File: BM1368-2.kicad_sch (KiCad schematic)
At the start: 39 parts, among them U12 BM1368_mode1, U13 BM1368_mode1

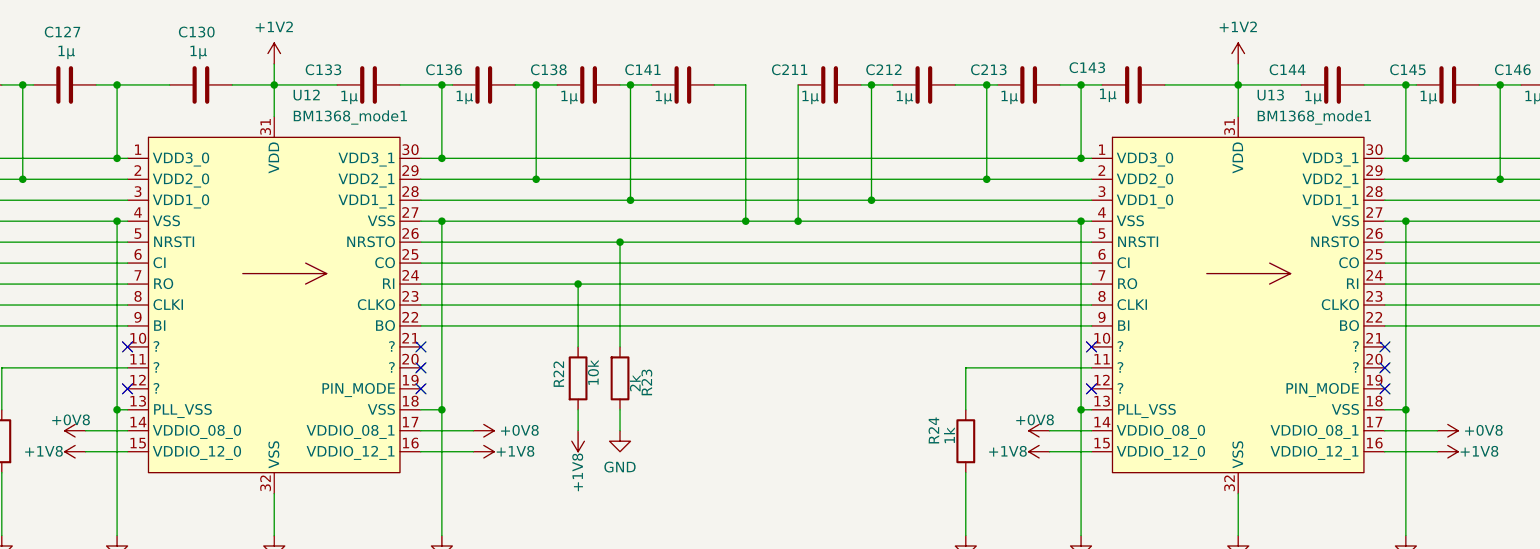
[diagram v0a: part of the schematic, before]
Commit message: Added 4th Phase Buck
Started to add 4th Phase for the Buck, implementing BM1370 footprint etc
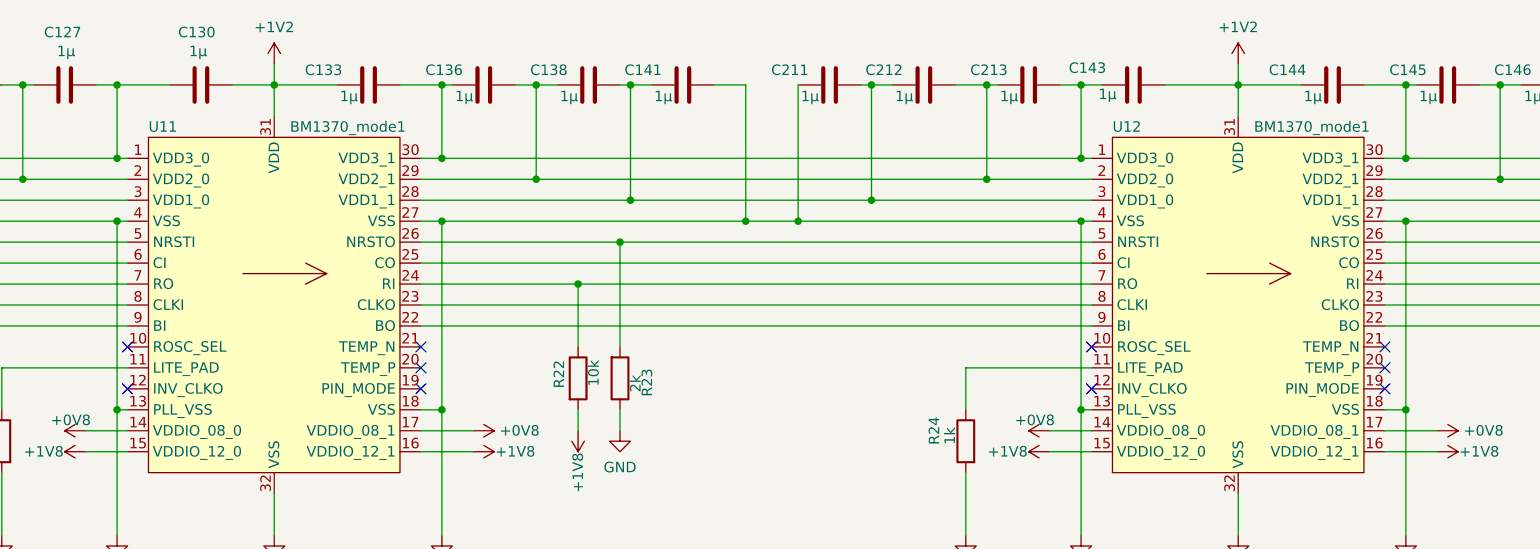
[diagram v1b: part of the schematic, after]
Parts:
- removed U12, U13: BM1368_mode1, myfootprints:bm1368-package-modified, symbol mylib7:BM1368_mode1
- added U11, U12: BM1370_mode1, Nerd8:BM1370, symbol bitaxe:BM1370_mode1
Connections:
- net +0V8: now also U11.14 (VDDIO_08_0), U11.17 (VDDIO_08_1), U12.14 (VDDIO_08_0), U12.17 (VDDIO_08_1)
- net +1V2: now also U11.31 (VDD), U12.31 (VDD)
- net +1V8: now also U11.15 (VDDIO_12_0), U11.16 (VDDIO_12_1), U12.15 (VDDIO_12_0), U12.16 (VDDIO_12_1)
- net BI: now also U11.9 (BI)
- net BO: now also U12.22 (BO)
- net CI: now also U11.6 (CI)
- net CLKI: now also U11.8 (CLKI)
- net CLKO: now also U12.23 (CLKO)
- net CO: now also U12.25 (CO)
- net GND: now also U11.13 (PLL_VSS), U11.18 (VSS), U11.27 (VSS), U11.32 (VSS), U11.4 (VSS), U12.13 (PLL_VSS), U12.18 (VSS), U12.27 (VSS), U12.32 (VSS), U12.4 (VSS)
- net NRSTI: now also U11.5 (NRSTI)
- net NRSTO: now also U12.26 (NRSTO)
- net RI: now also U12.24 (RI)
- net RO: now also U11.7 (RO)
- net U11-VDD1_1: now also U11.3 (VDD1_0)
- net U11-VDD2_1: now also U11.2 (VDD2_0)
- net U11-VDD3_1: now also U11.1 (VDD3_0)
- net U13-VDD1_1: now also U12.28 (VDD1_1)
- net U13-VDD2_1: now also U12.29 (VDD2_1)
- net U13-VDD3_1: now also U12.30 (VDD3_1)
- net at C133.2, C136.1, C143.1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: now also U11.30 (VDD3_1), U12.1 (VDD3_0)
- net at C136.2, C138.1, C212.2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: now also U11.29 (VDD2_1), U12.2 (VDD2_0)
- net at C138.2, C141.1, C211.2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: now also U11.28 (VDD1_1), U12.3 (VDD1_0)
- net at R24.1: now also U12.11 (LITE_PAD)
- net at R23.2: now also U11.26 (NRSTO), U12.5 (NRSTI)
- net at R22.1: now also U11.24 (RI), U12.7 (RO)
- net at R21.1: now also U11.11 (LITE_PAD)
- new net: U11.25 (CO), U12.6 (CI)
- new net: U11.23 (CLKO), U12.8 (CLKI)
- new net: U11.22 (BO), U12.9 (BI)

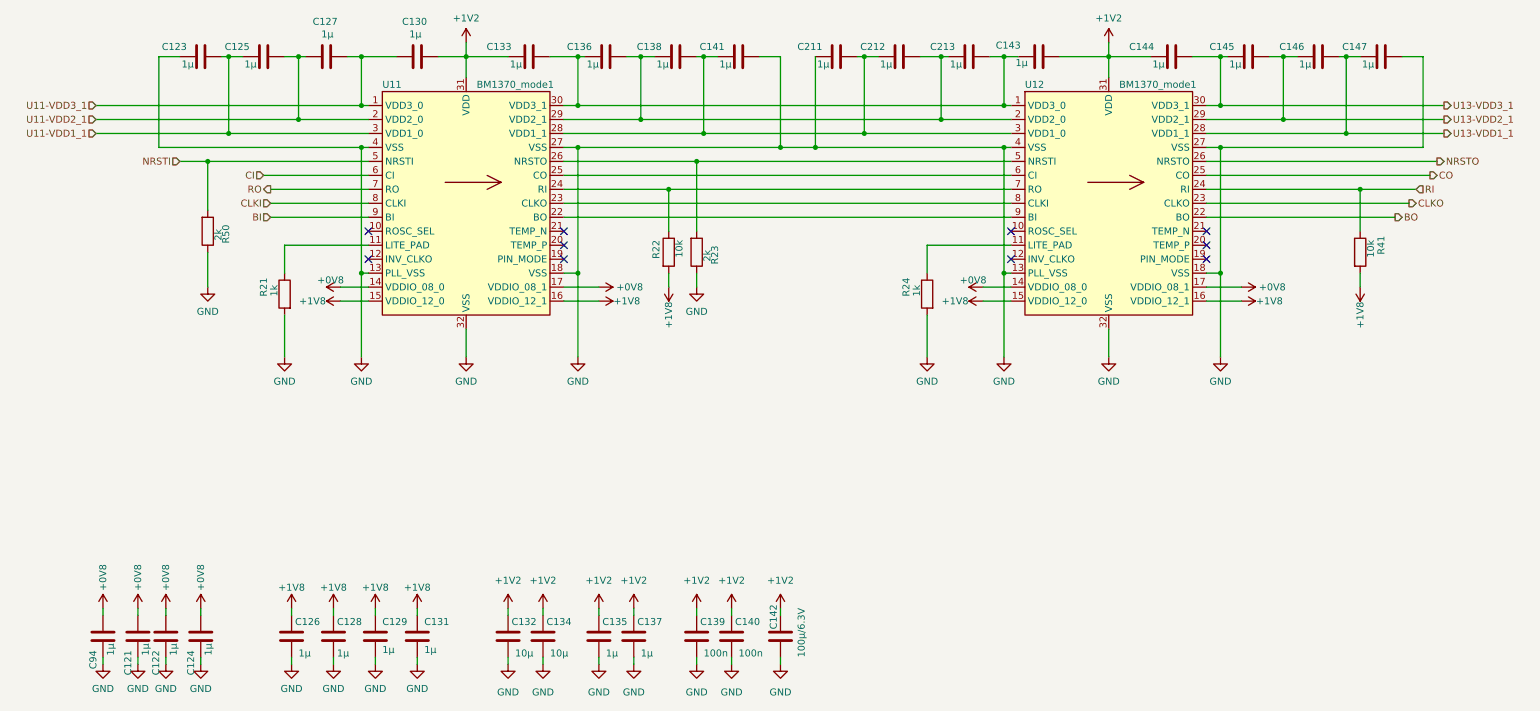
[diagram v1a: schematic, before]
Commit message: Changed LDO to 1V2 and original 1V2 to VDD
1V8 LDO replaced with 1V2 LDO
Crystal replaced
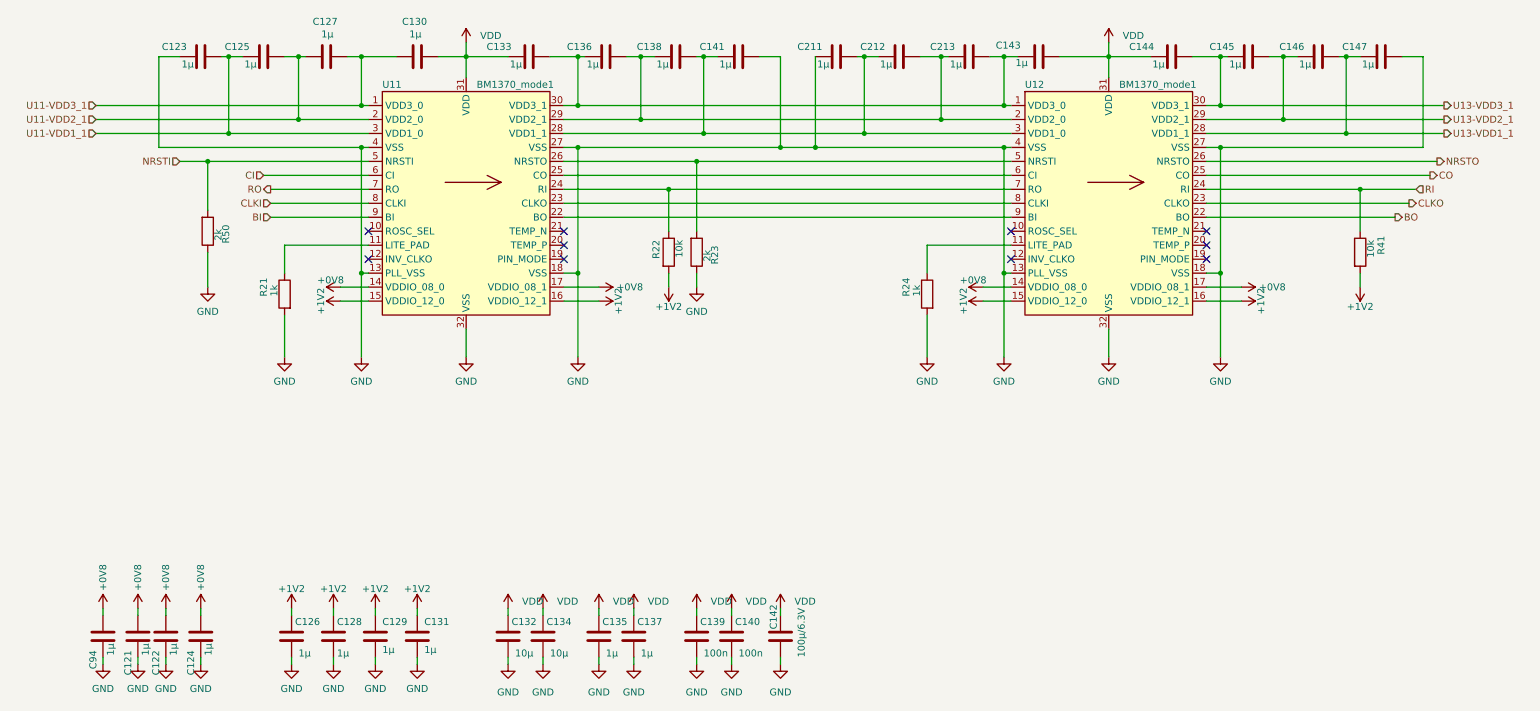
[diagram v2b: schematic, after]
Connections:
- net +1V8 is gone; now on net +1V2: C126.1, C128.1, C129.1, C131.1, R22.2, R41.2, U11.15 (VDDIO_12_0), U11.16 (VDDIO_12_1), U12.15 (VDDIO_12_0), U12.16 (VDDIO_12_1)
- net +1V2: no longer C130.2, C132.1, C133.1, C134.1, C135.1, C137.1, C139.1, C140.1, C142.1, C143.2, C144.1, U11.31 (VDD), U12.31 (VDD)
- new net VDD: C130.2, C132.1, C133.1, C134.1, C135.1, C137.1, C139.1, C140.1, C142.1, C143.2, C144.1, U11.31 (VDD), U12.31 (VDD)

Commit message: BOM specifications
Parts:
- C121, C122, C123, C124, C125, C126, C127, C128, C129, C130, C131, C133, C135, C136, C137, C138, C141, C143, C144, C145, C146, C147, C211, C212, C213, C94: value 1µ -> 1µ/25V; Brand (none) -> Samsung Electro-Mechanics; Distributor (none) -> D; Manufacturer (none) -> CL21B105KAFNNNE; OrderNr (none) -> 1276-1066-1-ND; Size (none) -> 0805
- C132, C134: value 10µ -> 10µ/25V; Brand (none) -> TDK Corporation; Size (none) -> 0805
- C139, C140: value 100n -> 100n/0.7mm; Brand (none) -> YAGEO; Distributor (none) -> D; Manufacturer (none) -> AC0805KRX7R9BB104; OrderNr (none) -> 311-3037-1-ND; Size (none) -> 0805
- C142: Brand (none) -> KEMET; Size (none) -> 1210
- R21, R24: Brand (none) -> Stackpole Electronics Inc; Distributor (none) -> D; Manufacturer (none) -> RNCP0805FTD1K00; OrderNr (none) -> RNCP0805FTD1K00CT-ND; Size (none) -> 0805
- R22, R41: Brand (none) -> Stackpole Electronics Inc; Distributor (none) -> D; Manufacturer (none) -> RMCF0805FT10K0; OrderNr (none) -> RMCF0805FT10K0CT-ND; Size (none) -> 0805
- R23, R50: Brand (none) -> TE Connectivity Passive Product; Distributor (none) -> D; Manufacturer (none) -> CRG0805F2K0; OrderNr (none) -> A126358CT-ND; Size (none) -> 0805
- U11, U12: Manufacturer (none) -> BITMAIN BM1370 ASIC
